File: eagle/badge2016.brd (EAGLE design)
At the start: 135 x 100.5 mm, 128 parts, among them IC1 25AA080SN, IC2 FT231XQ, J1 USB-MICRO, Q2 BC857ALT1SMD, Q2_24MHZ NX5032G, X1 PASSER-07, X10 PAD-1.27X1.27, X11 PAD-1.27X1.27, X12 PAD-1.27X1.27, X13 PAD-1.27X1.27, X14 PAD-1.27X1.27, X15 PAD-1.27X1.27, X16 PAD-1.27X1.27, X17 PAD-1.27X1.27, X18 PAD-1.27X1.27, X19 PAD-1.27X1.27, X2 PASSER-07, X20 PAD-1.27X1.27, X21 PAD-0.5, X3 PASSER-07, X4 PAD-0.5, X5 PAD-0.5, X6 PAD-0.5, X7 PAD-0.5, X8 PAD-1.27X1.27, X9 PAD-1.27X1.27

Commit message: final pcb layout + schematic
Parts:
- removed NC_BLBD_3V3, NC_BLBD_GND, NC_BLBD_PD, NC_BLBD_PU: (no value), we-rcl:C0402
- removed X11, X8, X9: PAD-1.27X1.27, we-rcl:PAD-1.27X1.27
- added B_LOADER_PDWN: 10k, we-rcl:C0402
- added U$7: YELLOW_BUSH, ERNW_parts:YELLOW_BUSH
- L1: device we-rcl:C0402 -> we-rcl:C0603
- moved X10 3.55 mm to (34.7, 67.3)
- moved NC_R18 2.35 mm to (54.6, 81.4)
- moved NC_R19 2.35 mm to (54.6, 82.5)
- moved X16 2.05 mm to (38.0, 66.6), turned to 90 degrees
- renumbered NC-U$13 to BTN_RESET, NC_BOOTLOADER_BTN to BOOTLOADER_BTN, R13 to NC_R13, R14 to NC_R14
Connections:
- removed net N$33: NC_R14.1, U$11.4
- removed net N$55: BOOTLOADER_BTN.A1, BOOTLOADER_BTN.A2, NC_BLBD_3V3.2, NC_BLBD_GND.2
- net 3V3: now also BOOTLOADER_BTN.A1, BOOTLOADER_BTN.A2; no longer NC_BLBD_3V3.1, NC_BLBD_PU.1
- net BOOTLOADER_BACKDOOR: now also B_LOADER_PDWN.2; no longer NC_BLBD_PD.2, NC_BLBD_PU.2
- net GND: now also B_LOADER_PDWN.1; no longer NC_BLBD_GND.1, NC_BLBD_PD.1, X11.1
- net N$25: no longer X8.1
- net N$30: now also NC_R14.1, U$11.4
- net N$32: no longer X9.1
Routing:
- net N$55: track 12.1 -> 0.00 mm
- net 3V3: track 319.6 -> 325.8 mm
- net N$30: track 6.91 -> 10.6 mm
- net N$33: track 2.71 -> 0.00 mm
- net GND: track 209.3 -> 207.3 mm, vias 361 -> 358
- net N$25: track 12.9 -> 11.3 mm
- net N$32: track 11.6 -> 9.98 mm
- net BOOTLOADER_BACKDOOR: track 49.5 -> 48.3 mm
- net VUSB_IN: track 64.4 -> 65.1 mm
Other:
- board text added: "3v3 Disp"
- board text added: "3v3 Main"
- board text added: "BOOTLOADER"
- board text added: "CC1310"
- board text added: "FT231X"
- board text added: "For OnBoard Antenna"
- board text added: "For SMA Antenna"
- board text added: "Interface"
- board text added: "LTC3554"
- board text added: "Lanyard"
- board text added: "SPI Flash"
- board text removed: "BAT+"
- board text removed: "OnBoard Antenna"
- board text removed: "SMA Antenna"

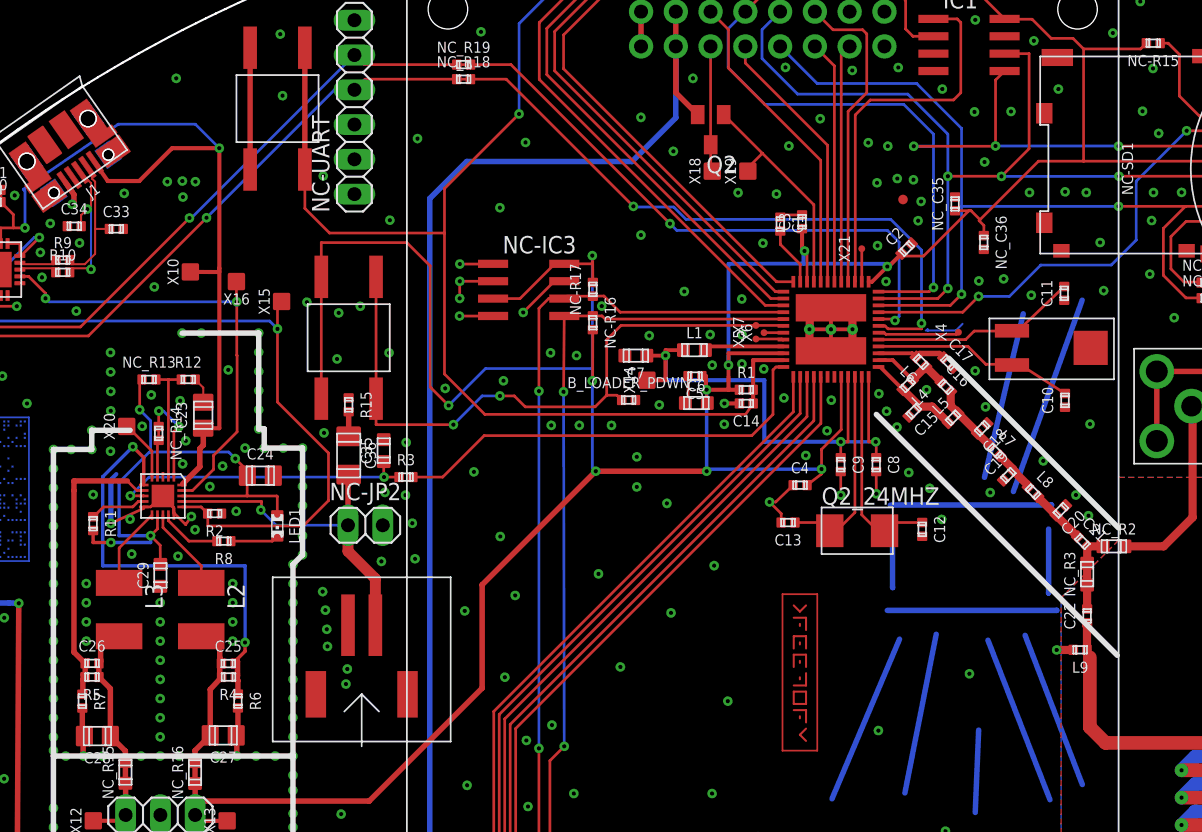
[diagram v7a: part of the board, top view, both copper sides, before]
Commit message: applied notes from watterott
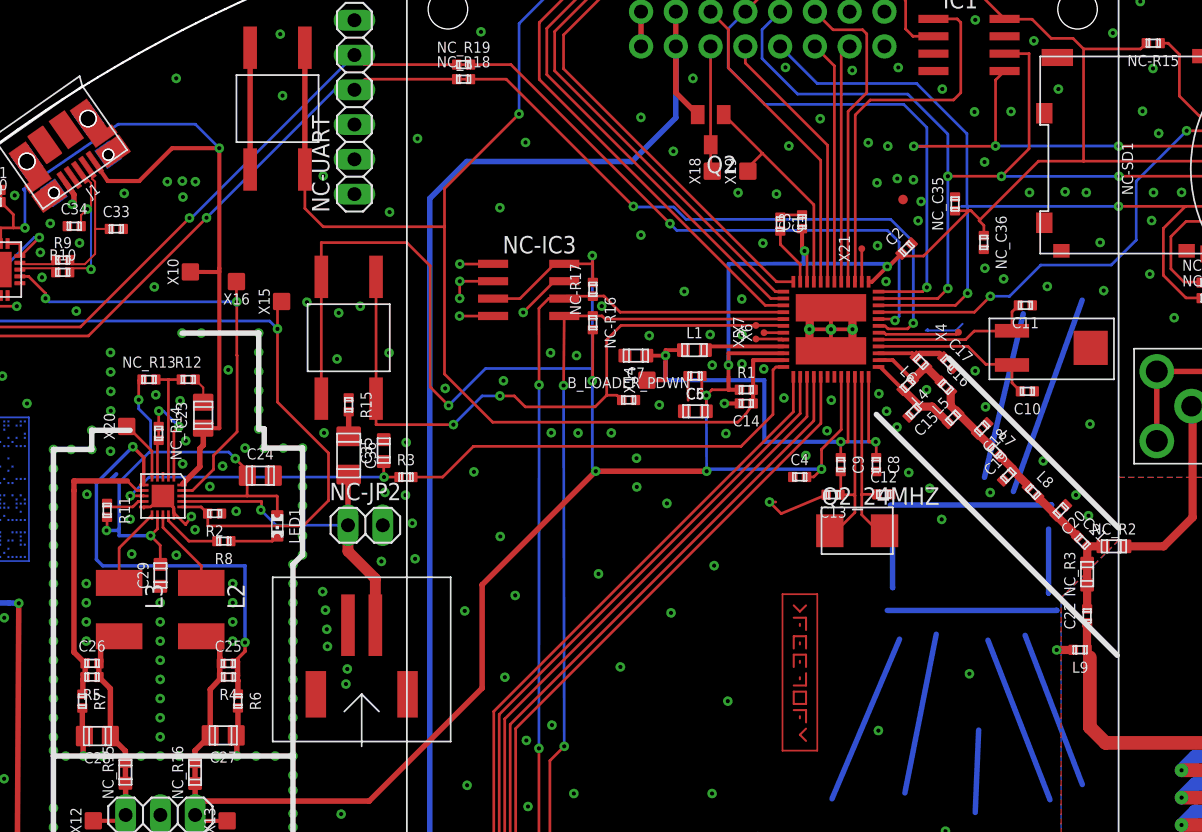
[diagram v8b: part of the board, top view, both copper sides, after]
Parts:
- moved C13 3.87 mm to (81.6, 51.0)
- moved C12 3.80 mm to (85.3, 51.1), turned to 270 degrees
- moved C11 2.97 mm to (95.7, 64.9), turned to 90 degrees
- moved C10 2.83 mm to (95.8, 58.6), turned to 90 degrees
- moved R11 1.41 mm to (28.6, 49.9)
- moved C6 0.60 mm to (71.6, 57.1)
- moved C4 0.60 mm to (79.2, 52.3)
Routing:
- net GND: track 207.3 -> 200.7 mm, vias 358 -> 354
- net V_USB: track 42.7 -> 39.2 mm
- net N$16: track 15.1 -> 12.0 mm
- net N$2: track 14.8 -> 12.5 mm
- net N$4: track 15.2 -> 13.3 mm
- net N$5: track 15.1 -> 13.4 mm
- net N$29: track 4.16 -> 2.95 mm
- net SPI_MOSI: track 83.4 -> 82.3 mm
- net FTDI_TXD: track 100.2 -> 99.1 mm
- net SPI_MISO: track 62.4 -> 63.0 mm
